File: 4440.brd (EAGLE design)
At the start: 100 x 80 mm, 30 parts

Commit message: Completed the layout
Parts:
- C1: value 1000uf -> 4700uf
- C13, C16: device rcl:E3,5-8 -> rcl:E7,5-16
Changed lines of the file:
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@@
 </autorouter>
 <elements>
-<element name="C1" library="rcl" package="E7,5-16" value="1000uf" x="17.78" y="31.75"/>
+<element name="C1" library="rcl" package="E7,5-16" value="4700uf" x="17.78" y="31.75"/>
 <element name="J1" library="SparkFun-Connectors" package="1X07_LONGPADS" value="" x="36.83" y="76.2"/>
 <element name="J2" library="SparkFun-Connectors" package="1X07_LONGPADS" value="" x="54.61" y="76.2"/>
@@
 <element name="C11" library="rcl" package="E3,5-8" value="220uf" x="5.08" y="-115.57"/>
 <element name="C12" library="rcl" package="E3,5-8" value="100uf" x="5.08" y="-124.46"/>
-<element name="C13" library="rcl" package="E3,5-8" value="1000uf" x="5.08" y="-133.35"/>
+<element name="C13" library="rcl" package="E7,5-16" value="1000uf" x="5.08" y="-133.35"/>
 <element name="R1" library="resistor" package="0207/12" value="4.7ohm" x="-6.35" y="-140.97"/>
 <element name="C14" library="rcl" package="C050-055X075" value="" x="-10.16" y="-147.32"/>
 <element name="C15" library="rcl" package="E3,5-8" value="100uf" x="0" y="-154.94"/>
-<element name="C16" library="rcl" package="E3,5-8" value="1000uf" x="-8.89" y="-166.37"/>
+<element name="C16" library="rcl" package="E7,5-16" value="1000uf" x="-8.89" y="-166.37"/>
 <element name="R2" library="resistor" package="0207/12" value="4.7ohm" x="-6.35" y="-173.99"/>
 <element name="C17" library="rcl" package="C050-055X075" value="" x="2.54" y="-167.64"/>
@@
 <contactref element="C13" pad="+"/>
 <wire x1="6.858" y1="-124.46" x2="59.69" y2="76.2" width="0" layer="19" extent="1-1"/>
-<wire x1="3.302" y1="-133.35" x2="6.858" y2="-124.46" width="0" layer="19" extent="1-1"/>
+<wire x1="1.27" y1="-133.35" x2="6.858" y2="-124.46" width="0" layer="19" extent="1-1"/>
 </signal>
 <signal name="N$11">
@@
 <wire x1="-7.62" y1="-147.32" x2="-11.43" y2="-194.31" width="0" layer="19" extent="1-1"/>
 <wire x1="0" y1="-140.97" x2="-7.62" y2="-147.32" width="0" layer="19" extent="1-1"/>
-<wire x1="6.858" y1="-133.35" x2="0" y2="-140.97" width="0" layer="19" extent="1-1"/>
+<wire x1="8.89" y1="-133.35" x2="0" y2="-140.97" width="0" layer="19" extent="1-1"/>
 </signal>
 <signal name="N$15">
@@
 <contactref element="C15" pad="-"/>
 <contactref element="C16" pad="+"/>
-<wire x1="1.778" y1="-154.94" x2="-10.668" y2="-166.37" width="0" layer="19" extent="1-1"/>
+<wire x1="1.778" y1="-154.94" x2="-12.7" y2="-166.37" width="0" layer="19" extent="1-1"/>
 <wire x1="64.77" y1="76.2" x2="1.778" y2="-154.94" width="0" layer="19" extent="1-1"/>
 </signal>
@@
 <wire x1="0" y1="-173.99" x2="-11.43" y2="-201.93" width="0" layer="19" extent="1-1"/>
 <wire x1="5.08" y1="-167.64" x2="0" y2="-173.99" width="0" layer="19" extent="1-1"/>
-<wire x1="-7.112" y1="-166.37" x2="0" y2="-173.99" width="0" layer="19" extent="1-1"/>
+<wire x1="-5.08" y1="-166.37" x2="0" y2="-173.99" width="0" layer="19" extent="1-1"/>
 </signal>
 </signals>

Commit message: Completed the project with PCB layout
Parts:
- moved J8 252.4 mm to (6.02, 42.3), turned to 90 degrees
- moved J5 251.2 mm to (5.64, 63.9), turned to 90 degrees
- moved J4 238.8 mm to (5.74, 59.1), turned to 270 degrees
- moved J7 235.8 mm to (73.4, 18.1), turned to 180 degrees
- moved C15 226.6 mm to (68.9, 60.9), turned to 180 degrees
- moved C16 224.4 mm to (71.3, 43.2)
- moved J6 222.0 mm to (53.2, 18.1)
- moved R2 219.5 mm to (71.8, 31.1)
- moved C17 205.2 mm to (71.8, 25.5)
- moved C12 193.6 mm to (60.4, 61.1)
- moved C14 184.5 mm to (54.9, 25.4), turned to 180 degrees
- moved C11 182.8 mm to (52.1, 61.1), turned to 270 degrees
- moved C13 182.6 mm to (52.6, 43.0), turned to 180 degrees
- moved R1 182.5 mm to (54.3, 31.2), turned to 180 degrees
- moved C10 173.4 mm to (14.2, 65.2), turned to 90 degrees
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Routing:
- net VCC: track 0.00 -> 112.6 mm, vias 0 -> 4
- net N$9: track 0.00 -> 59.2 mm, vias 0 -> 2
- net N$4: track 0.00 -> 57.0 mm
- net N$2: track 0.00 -> 33.5 mm
- net N$13: track 0.00 -> 33.4 mm
- net N$3: track 0.00 -> 33.0 mm
- net N$16: track 0.00 -> 30.8 mm
- net N$19: track 0.00 -> 30.1 mm
- net N$11: track 0.00 -> 27.5 mm
- net N$14: track 0.00 -> 13.4 mm
- net N$12: track 0.00 -> 12.5 mm
- net N$1: track 0.00 -> 11.0 mm
- net N$5: track 0.00 -> 10.6 mm
- net N$7: track 0.00 -> 10.2 mm
- net N$10: track 0.00 -> 10.1 mm
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- added copper zone on layer 16, net GND
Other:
- board size 100 x 80 mm -> 82.6 x 62 mm

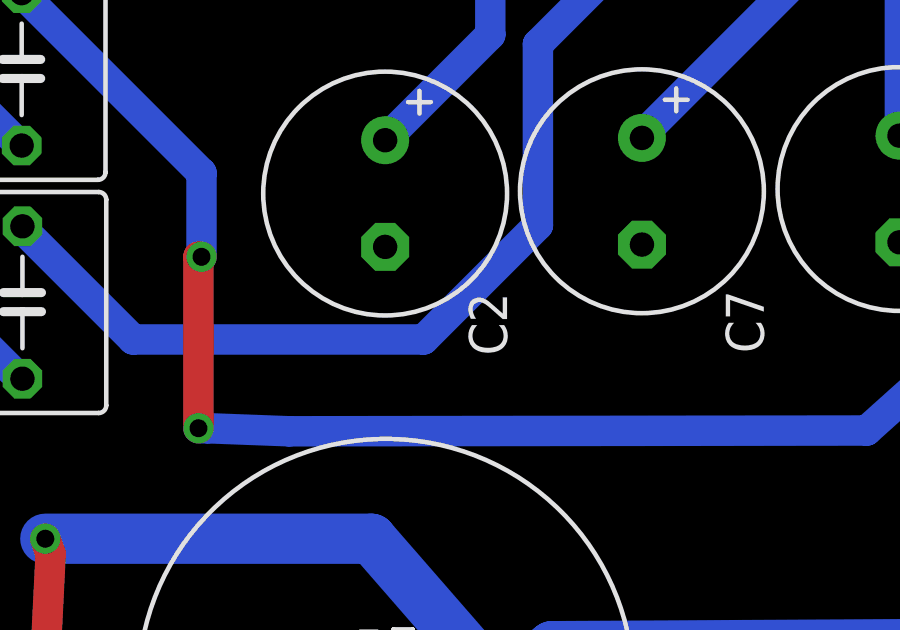
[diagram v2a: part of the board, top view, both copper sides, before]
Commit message: Fixed the last missing ground connection
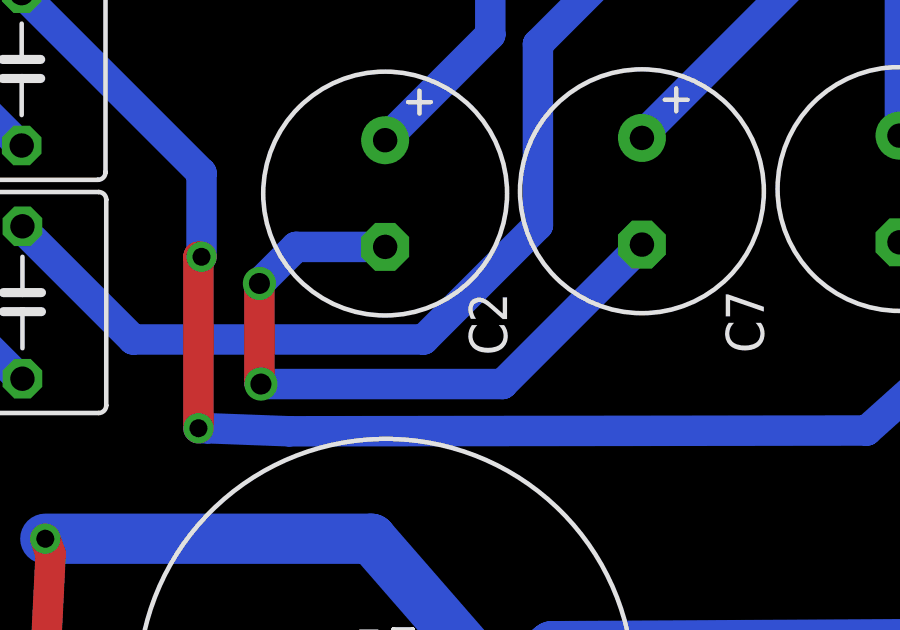
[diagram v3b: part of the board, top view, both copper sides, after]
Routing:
- net GND: track 0.00 -> 22.7 mm, vias 0 -> 2
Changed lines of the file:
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@@
 <vertex x="-3.5306" y="83.0326"/>
 </polygon>
-<wire x1="34.8996" y1="59.3598" x2="26.3398" y2="59.2836" width="0" layer="19" extent="1-1"/>
+<wire x1="34.8996" y1="59.3598" x2="30.2514" y2="54.7116" width="1.016" layer="16"/>
+<wire x1="30.2514" y1="54.7116" x2="22.1996" y2="54.7116" width="1.016" layer="16"/>
+<via x="22.1996" y="54.7116" extent="1-16" drill="0.7"/>
+<wire x1="22.1996" y1="54.7116" x2="22.1488" y2="54.7624" width="1.016" layer="1"/>
+<wire x1="22.1488" y1="54.7624" x2="22.1488" y2="58.0644" width="1.016" layer="1"/>
+<via x="22.1488" y="58.0644" extent="1-16" drill="0.7"/>
+<wire x1="22.1488" y1="58.0644" x2="23.368" y2="59.2836" width="1.016" layer="16"/>
+<wire x1="23.368" y1="59.2836" x2="26.3398" y2="59.2836" width="1.016" layer="16"/>
 </signal>
 <signal name="N$4">
